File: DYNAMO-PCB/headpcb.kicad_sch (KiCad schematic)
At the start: 17 parts, among them J10 Conn_01x03_Pin, J11 Conn_01x03_Pin, J12 Conn_01x03_Pin, J4 USB_C_Receptacle, J5 Conn_01x02_Pin, J6 Conn_01x03_Pin, J7 Conn_01x08_Socket, J8 Conn_01x03_Pin, J9 Conn_01x03_Pin

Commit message: 692122030100
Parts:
- removed J4: USB_C_Receptacle, symbol Connector:USB_C_Receptacle
- added J31: USB_C_Receptacle_USB2.0_16P, Connector_USB:USB_C_Receptacle_GCT_USB4105-xx-A_16P_TopMnt_Horizontal, symbol Connector:USB_C_Receptacle_USB2.0_16P
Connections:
- new net: J31.A1 (GND), J31.A12 (GND), J31.B1 (GND), J31.B12 (GND)
- new net: J31.A4 (VBUS), J31.A9 (VBUS), J31.B4 (VBUS), J31.B9 (VBUS)
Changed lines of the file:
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@@
-	)
-	(symbol
-		(lib_id "Connector:USB_C_Receptacle")
-		(at 62.23 93.98 0)
-		(unit 1)
-		(exclude_from_sim no)
-		(in_bom yes)
-		(on_board yes)
-		(dnp no)
-		(fields_autoplaced yes)
-		(property "Reference" "J4"
-			(at 62.23 60.96 0)
-			(effects
-				(font
-					(size 1.27 1.27)
-				)
-			)
-		)
-		(property "Value" "USB_C_Receptacle"
-			(at 62.23 63.5 0)
-			(effects
-				(font
-					(size 1.27 1.27)
-				)
-			)
-		)
-		(property "Footprint" ""
-			(at 66.04 93.98 0)
-			(effects
-				(font
-					(size 1.27 1.27)
-				)
-				(hide yes)
-			)
-		)
-		(property "Datasheet" "https://www.usb.org/sites/default/files/documents/usb_type-c.zip"
-			(at 66.04 93.98 0)
-			(effects
-				(font
-					(size 1.27 1.27)
-				)
-				(hide yes)
-			)
-		)
-		(property "Description" "USB Full-Featured Type-C Receptacle connector"
-			(at 62.23 93.98 0)
-			(effects
-				(font
-					(size 1.27 1.27)
-				)
-				(hide yes)
-			)
-		)
-		(pin "B8"
-		)
-		(pin "A8"
-		)
-		(pin "B2"
-		)
-		(pin "B12"
-		)
-		(pin "A12"
-		)
-		(pin "B5"
-		)
-		(pin "A7"
-		)
-		(pin "S1"
-		)
-		(pin "A3"
-		)
-		(pin "A10"
-		)
-		(pin "A11"
-		)
-		(pin "B3"
-		)
-		(pin "B10"
-		)
-		(pin "A4"
-		)
-		(pin "A1"
-		)
-		(pin "B6"
-		)
-		(pin "B1"
-		)
-		(pin "B7"
-		)
-		(pin "B9"
-		)
-		(pin "A9"
-		)
-		(pin "A6"
-		)
-		(pin "B4"
-		)
-		(pin "B11"
-		)
-		(pin "A2"
-		)
-		(pin "A5"
-		)
-		(instances
-			(project "DYNAMO-PCB"
-				(path "/2ca9dd43-411d-4cc5-8a4b-ed00d72bae91/8fd238d6-8885-491d-831e-5a6be755c492"
-					(reference "J4")
-					(unit 1)
-				)
-			)
-		)
 	)
 	(symbol
@@
 					(unit 1)
 				)
+			)
+		)
+	)
+	(symbol
+		(lib_id "Connector:USB_C_Receptacle_USB2.0_16P")
+		(at 63.5 104.14 0)
+		(unit 1)
+		(exclude_from_sim no)
+		(in_bom yes)
+		(on_board yes)
+		(dnp no)
+		(fields_autoplaced yes)
+		(property "Reference" "J31"
+			(at 63.5 81.28 0)
+			(effects
+				(font
+					(size 1.27 1.27)
+				)
+			)
+		)
+		(property "Value" "USB_C_Receptacle_USB2.0_16P"
+			(at 63.5 83.82 0)
+			(effects
+				(font
+					(size 1.27 1.27)
+				)
+			)
+		)
+		(property "Footprint" "Connector_USB:USB_C_Receptacle_GCT_USB4105-xx-A_16P_TopMnt_Horizontal"
+			(at 67.31 104.14 0)
+			(effects
+				(font
+					(size 1.27 1.27)
+				)
+				(hide yes)
+			)
+		)
+		(property "Datasheet" "https://www.usb.org/sites/default/files/documents/usb_type-c.zip"
+			(at 67.31 104.14 0)
+			(effects
+				(font
+					(size 1.27 1.27)
+				)
+				(hide yes)
+			)
+		)
+		(property "Description" "USB 2.0-only 16P Type-C Receptacle connector"
+			(at 63.5 104.14 0)
+			(effects
+				(font
+					(size 1.27 1.27)
+				)
+				(hide yes)
+			)
+		)
+		(pin "A1"
+		)
+		(pin "B12"
+		)
+		(pin "B9"
+		)
+		(pin "A4"
+		)
+		(pin "S1"
+		)
+		(pin "A12"
+		)
+		(pin "B1"
+		)
+		(pin "A9"
+		)
+		(pin "B4"
+		)
+		(pin "A7"
+		)
+		(pin "A5"
+		)
+		(pin "B6"
+		)
+		(pin "B5"
+		)
+		(pin "B8"
+		)
+		(pin "B7"
+		)
+		(pin "A6"
+		)
+		(pin "A8"
+		)
+		(instances
+			(project "DYNAMO-PCB"
+				(path "/2ca9dd43-411d-4cc5-8a4b-ed00d72bae91/8fd238d6-8885-491d-831e-5a6be755c492"
+					(reference "J31")
+					(unit 1)
+				)

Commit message: footprint assignments
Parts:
- C2, C3, C4, C5, C6, C7: footprint (none) -> Capacitor_THT:CP_Radial_D10.0mm_P5.00mm
- J10, J11, J12, J6, J8, J9: footprint (none) -> Connector_PinHeader_2.54mm:PinHeader_1x03_P2.54mm_Vertical
- J5: footprint (none) -> Connector_PinHeader_2.54mm:PinHeader_1x02_P2.54mm_Vertical
- J7: footprint (none) -> Connector_PinSocket_2.54mm:PinSocket_1x08_P2.54mm_Horizontal
- R2, R3: footprint (none) -> Resistor_THT:R_Axial_DIN0309_L9.0mm_D3.2mm_P12.70mm_Horizontal
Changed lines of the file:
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@@
 			)
 		)
-		(property "Footprint" ""
+		(property "Footprint" "Connector_PinSocket_2.54mm:PinSocket_1x08_P2.54mm_Horizontal"
 			(at 110.49 105.41 0)
 			(effects
@@
 			)
 		)
-		(property "Footprint" ""
+		(property "Footprint" "Resistor_THT:R_Axial_DIN0309_L9.0mm_D3.2mm_P12.70mm_Horizontal"
 			(at 125.222 137.16 90)
 			(effects
@@
 			)
 		)
-		(property "Footprint" ""
+		(property "Footprint" "Capacitor_THT:CP_Radial_D10.0mm_P5.00mm"
 			(at 108.9152 129.54 0)
 			(effects
@@
 			)
 		)
-		(property "Footprint" ""
+		(property "Footprint" "Connector_PinHeader_2.54mm:PinHeader_1x02_P2.54mm_Vertical"
 			(at 106.68 74.93 0)
 			(effects
@@
 			)
 		)
-		(property "Footprint" ""
+		(property "Footprint" "Connector_PinHeader_2.54mm:PinHeader_1x03_P2.54mm_Vertical"
 			(at 156.21 88.9 0)
 			(effects
@@
 			)
 		)
-		(property "Footprint" ""
+		(property "Footprint" "Connector_PinHeader_2.54mm:PinHeader_1x03_P2.54mm_Vertical"
 			(at 173.99 88.9 0)
 			(effects
@@
 			)
 		)
-		(property "Footprint" ""
+		(property "Footprint" "Capacitor_THT:CP_Radial_D10.0mm_P5.00mm"
 			(at 144.4752 129.54 0)
 			(effects
@@
 			)
 		)
-		(property "Footprint" ""
+		(property "Footprint" "Capacitor_THT:CP_Radial_D10.0mm_P5.00mm"
 			(at 160.9852 129.54 0)
 			(effects
@@
 			)
 		)
-		(property "Footprint" ""
+		(property "Footprint" "Capacitor_THT:CP_Radial_D10.0mm_P5.00mm"
 			(at 127.9652 129.54 0)
 			(effects
@@
 			)
 		)
-		(property "Footprint" ""
+		(property "Footprint" "Connector_PinHeader_2.54mm:PinHeader_1x03_P2.54mm_Vertical"
 			(at 106.68 88.9 0)
 			(effects
@@
 			)
 		)
-		(property "Footprint" ""
+		(property "Footprint" "Connector_PinHeader_2.54mm:PinHeader_1x03_P2.54mm_Vertical"
 			(at 139.7 88.9 0)
 			(effects
@@
 			)
 		)
-		(property "Footprint" ""
+		(property "Footprint" "Connector_PinHeader_2.54mm:PinHeader_1x03_P2.54mm_Vertical"
 			(at 190.5 88.9 0)
 			(effects
@@
 			)
 		)
-		(property "Footprint" ""
+		(property "Footprint" "Capacitor_THT:CP_Radial_D10.0mm_P5.00mm"
 			(at 178.7652 129.54 0)
 			(effects
@@
 			)
 		)
-		(property "Footprint" ""
+		(property "Footprint" "Resistor_THT:R_Axial_DIN0309_L9.0mm_D3.2mm_P12.70mm_Horizontal"
 			(at 106.172 137.16 90)
 			(effects
@@
 			)
 		)
-		(property "Footprint" ""
+		(property "Footprint" "Capacitor_THT:CP_Radial_D10.0mm_P5.00mm"
 			(at 195.2752 129.54 0)
 			(effects
@@
 			)
 		)
-		(property "Footprint" ""
+		(property "Footprint" "Connector_PinHeader_2.54mm:PinHeader_1x03_P2.54mm_Vertical"
 			(at 123.19 88.9 0)
 			(effects

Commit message: schematic wip
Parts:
- removed C2, C3, C4, C5, C6, C7: C_Polarized, Capacitor_THT:CP_Radial_D10.0mm_P5.00mm, symbol Device:C_Polarized
- removed R2, R3: R, Resistor_THT:R_Axial_DIN0309_L9.0mm_D3.2mm_P12.70mm_Horizontal, symbol Device:R
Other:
- moved on the sheet: J10, J11, J12, J31, J5, J6, J7, J8, J9

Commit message: schematic wip
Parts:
- added C2, C3, C4, C5: C_Polarized, Capacitor_THT:CP_Radial_D10.0mm_P5.00mm, symbol Device:C_Polarized
- added R2, R3: R, Resistor_THT:R_Axial_DIN0309_L9.0mm_D3.2mm_P12.70mm_Horizontal, symbol Device:R

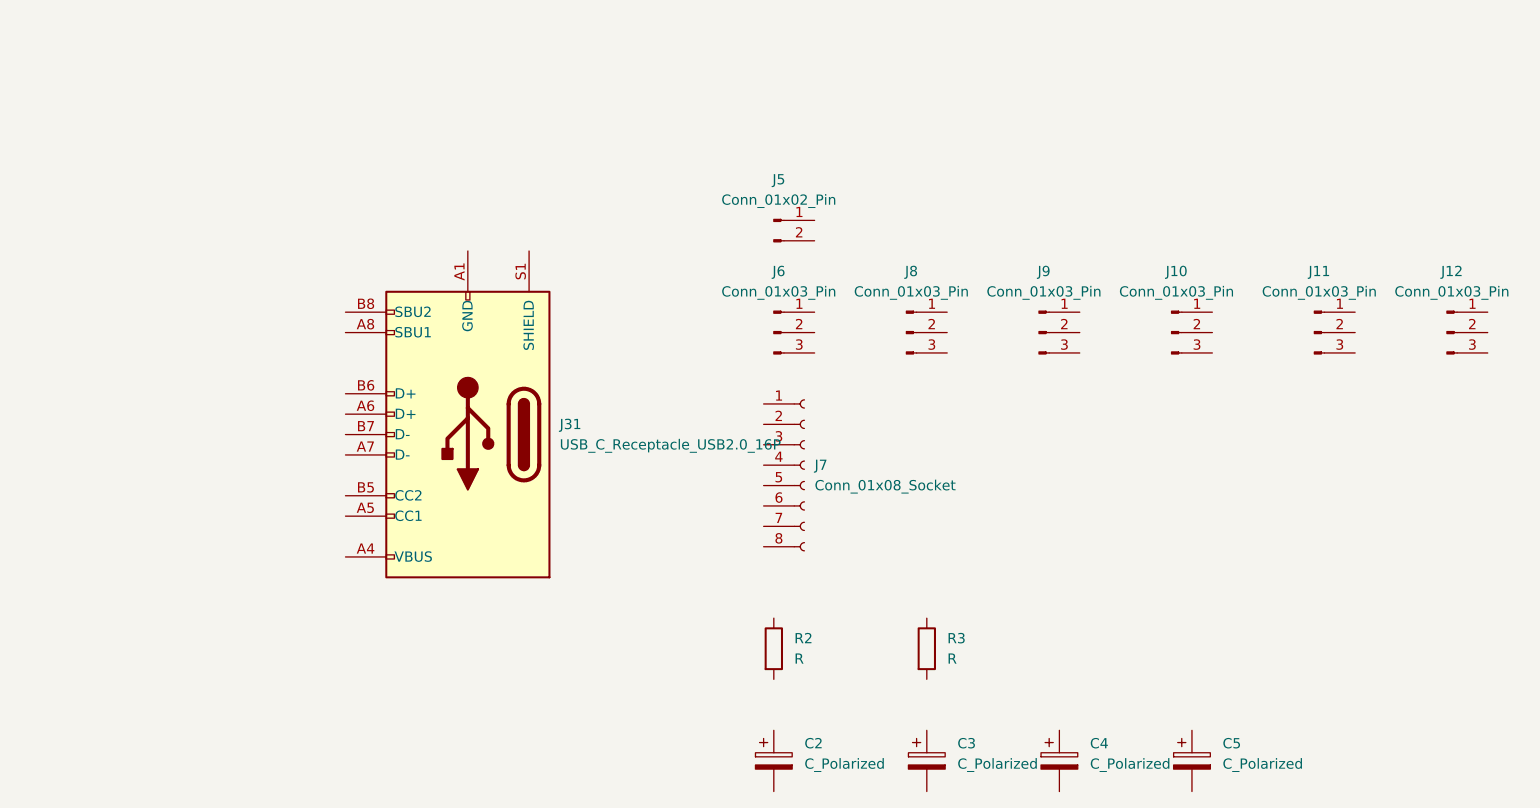
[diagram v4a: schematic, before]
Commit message: removed unncessary ic
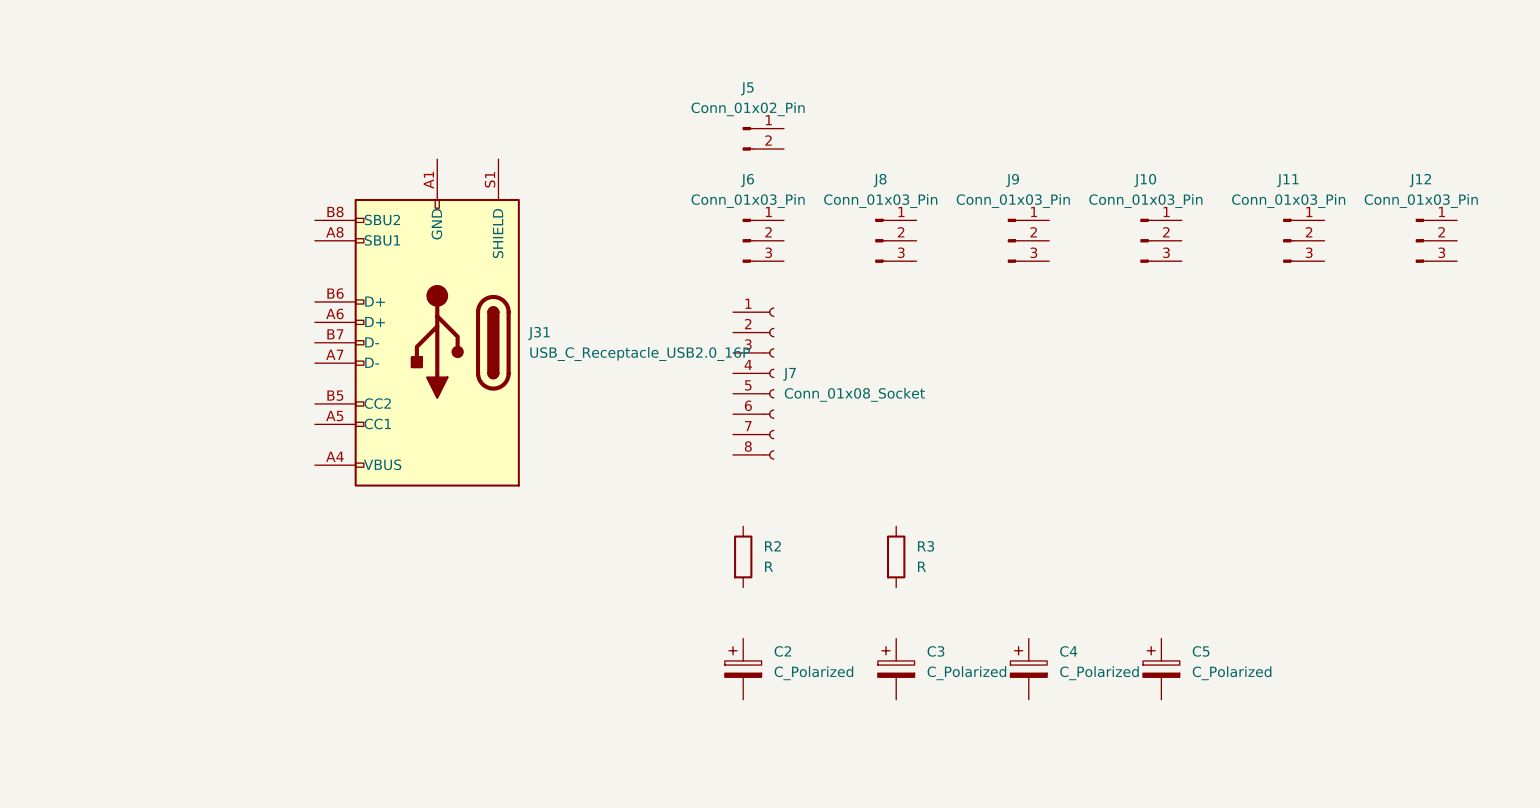
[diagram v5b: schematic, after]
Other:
- moved on the sheet: C2, C3, C4, C5, J10, J11, J12, J31, J5, J6, J7, J8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

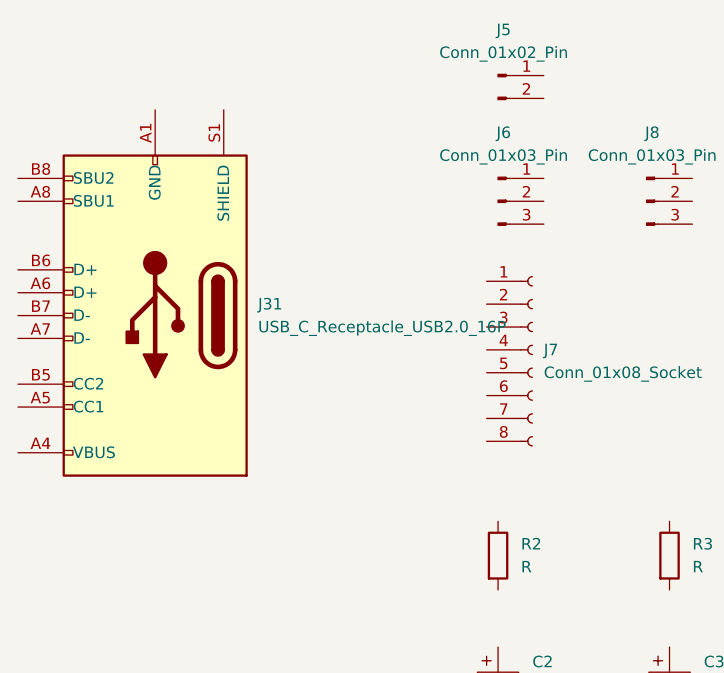
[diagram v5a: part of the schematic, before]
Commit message: removed usb7206
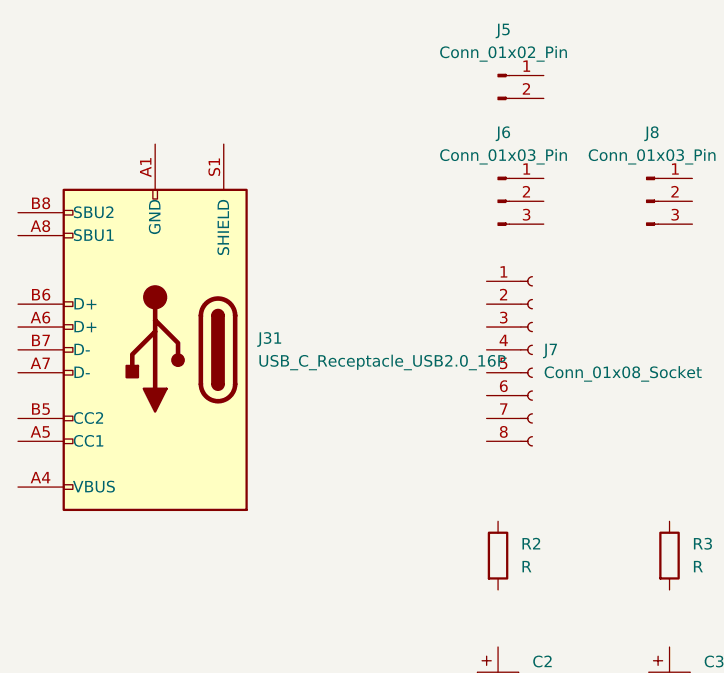
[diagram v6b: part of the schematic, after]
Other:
- moved on the sheet: J31
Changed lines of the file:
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@@
 	(symbol
 		(lib_id "Connector:USB_C_Receptacle_USB2.0_16P")
-		(at 99.06 92.71 180)
+		(at 99.06 96.52 180)
 		(unit 1)
 		(exclude_from_sim no)
@@
 		(fields_autoplaced yes)
 		(property "Reference" "J31"
-			(at 110.49 91.4399 0)
+			(at 110.49 95.2499 0)
 			(effects
 				(font
@@
 		)
 		(property "Value" "USB_C_Receptacle_USB2.0_16P"
-			(at 110.49 93.9799 0)
+			(at 110.49 97.7899 0)
 			(effects
 				(font
@@
 		)
 		(property "Footprint" "Connector_USB:USB_C_Receptacle_GCT_USB4105-xx-A_16P_TopMnt_Horizontal"
-			(at 95.25 92.71 0)
+			(at 95.25 96.52 0)
 			(effects
 				(font
@@
 		)
 		(property "Datasheet" "https://www.usb.org/sites/default/files/documents/usb_type-c.zip"
-			(at 95.25 92.71 0)
+			(at 95.25 96.52 0)
 			(effects
 				(font
@@
 		)
 		(property "Description" "USB 2.0-only 16P Type-C Receptacle connector"
-			(at 99.06 92.71 0)
+			(at 99.06 96.52 0)
 			(effects
 				(font

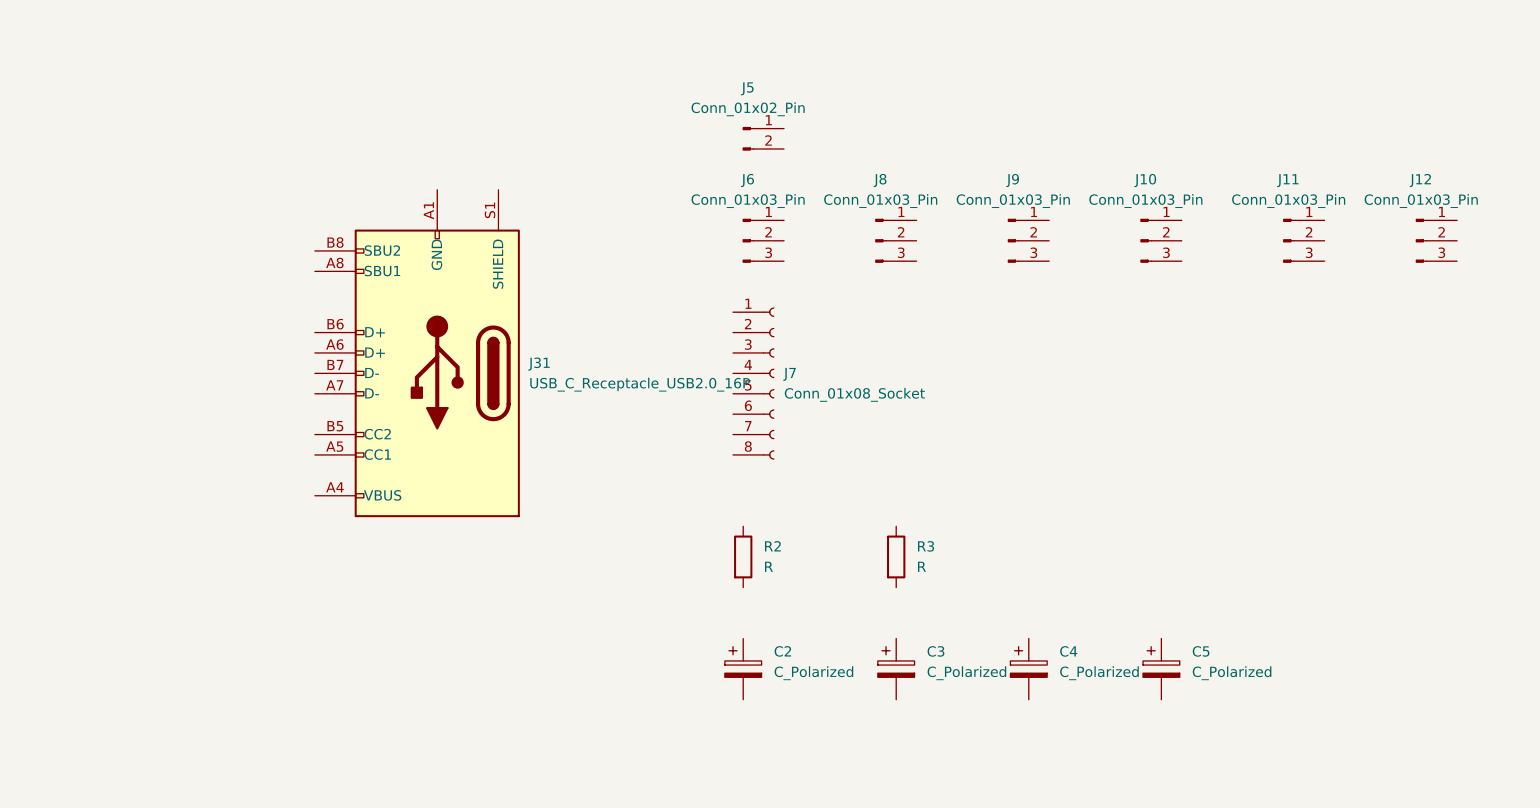
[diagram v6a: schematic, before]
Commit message: wired headpcb sch
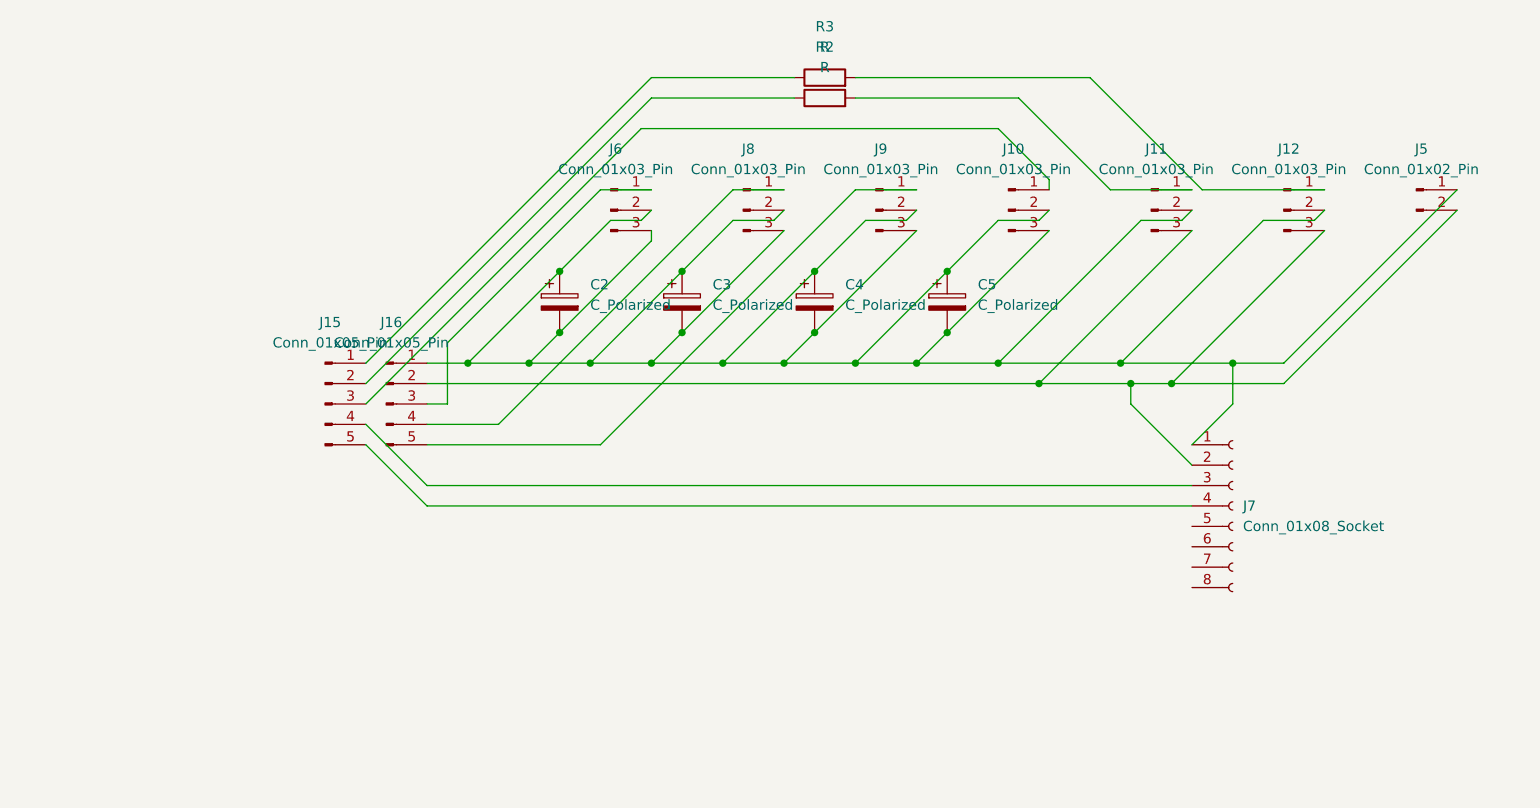
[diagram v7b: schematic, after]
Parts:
- removed J31: USB_C_Receptacle_USB2.0_16P, Connector_USB:USB_C_Receptacle_GCT_USB4105-xx-A_16P_TopMnt_Horizontal, symbol Connector:USB_C_Receptacle_USB2.0_16P
- added J15, J16: Conn_01x05_Pin, Connector_PinHeader_2.54mm:PinHeader_1x05_P2.54mm_Vertical, symbol Connector:Conn_01x05_Pin
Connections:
- net at J7.1 (Pin_1): now also C2.1, C2.2, C3.1, C3.2, C4.1, C4.2, C5.1, C5.2, J10.2 (Pin_2), J10.3 (Pin_3), J11.2 (Pin_2), J12.2 (Pin_2), J5.1 (Pin_1), J6.2 (Pin_2), J6.3 (Pin_3), J8.2 (Pin_2), J8.3 (Pin_3), J9.2 (Pin_2), J9.3 (Pin_3), J16.1 (Pin_1)
- net at J7.2 (Pin_2): now also J11.3 (Pin_3), J12.3 (Pin_3), J5.2 (Pin_2), J16.2 (Pin_2)
- net at J7.3 (Pin_3): now also J15.4 (Pin_4)
- net at J7.4 (Pin_4): now also J15.5 (Pin_5)
- net at R3.1: now also J15.1 (Pin_1)
- net at R3.2: now also J12.1 (Pin_1)
- net at J10.1 (Pin_1): now also J15.3 (Pin_3)
- net at J11.1 (Pin_1): now also R2.2
- net at J6.1 (Pin_1): now also J16.3 (Pin_3)
- net at J9.1 (Pin_1): now also J16.5 (Pin_5)
- net at R2.1: now also J15.2 (Pin_2)
- net at J8.1 (Pin_1): now also J16.4 (Pin_4)
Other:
- moved on the sheet: C2, C3, C4, C5, J10, J11, J12, J5, J6, J7, J8, J9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

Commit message: schematic wip
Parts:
- removed J15, J16: Conn_01x05_Pin, Connector_PinHeader_2.54mm:PinHeader_1x05_P2.54mm_Vertical, symbol Connector:Conn_01x05_Pin
- added J33: Conn_02x05_Counter_Clockwise, Connector_PinHeader_2.54mm:PinHeader_2x05_P2.54mm_Vertical, symbol Connector_Generic:Conn_02x05_Counter_Clockwise
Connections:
- net at C2.1, C3.1, C4.1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: now also J33.10 (Pin_10); no longer C2.2, C3.2, C4.2, C5.2, J10.3 (Pin_3), J6.3 (Pin_3), J8.3 (Pin_3), J9.3 (Pin_3)
- net GND: now reaches J11.3 (Pin_3), J12.3 (Pin_3), J5.2 (Pin_2), J7.2 (Pin_2)
- net GND: now also C2.2, C3.2, C4.2, C5.2, J10.3 (Pin_3), J6.3 (Pin_3), J8.3 (Pin_3), J9.3 (Pin_3), J33.9 (Pin_9)
- net at J7.3 (Pin_3): now also J33.4 (Pin_4)
- net at J7.4 (Pin_4): now also J33.5 (Pin_5)
- net at J6.1 (Pin_1): now also J33.8 (Pin_8)
- net at J8.1 (Pin_1): now also J33.7 (Pin_7)
- net at J9.1 (Pin_1): now also J33.6 (Pin_6)
- net at R3.1: now also J33.1 (Pin_1)
- net at J10.1 (Pin_1): now also J33.3 (Pin_3)
- net at R2.1: now also J33.2 (Pin_2)
- no-connect marks 0 -> 4
